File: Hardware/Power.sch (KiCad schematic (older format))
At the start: 24 parts, among them U601 PAM2306AYPAA, U603 LDO-X2SON-1.2V, U604 LDO-X2SON-3.3V, U605 LDO-X2SON-2.5V

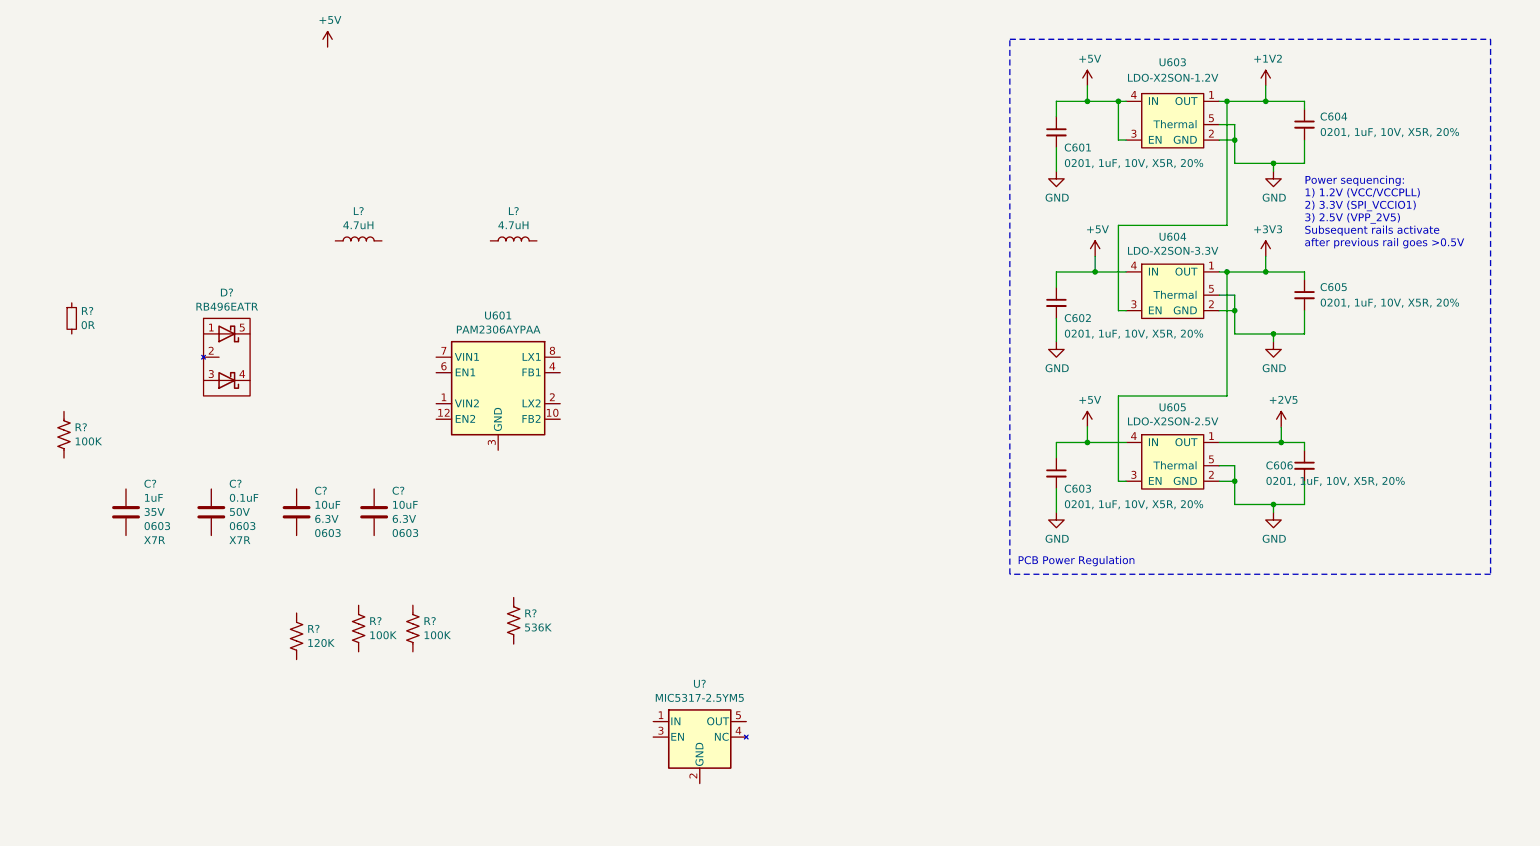
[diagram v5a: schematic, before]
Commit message: Prospecting the layout of AFE, detailing connectors to larger board size.
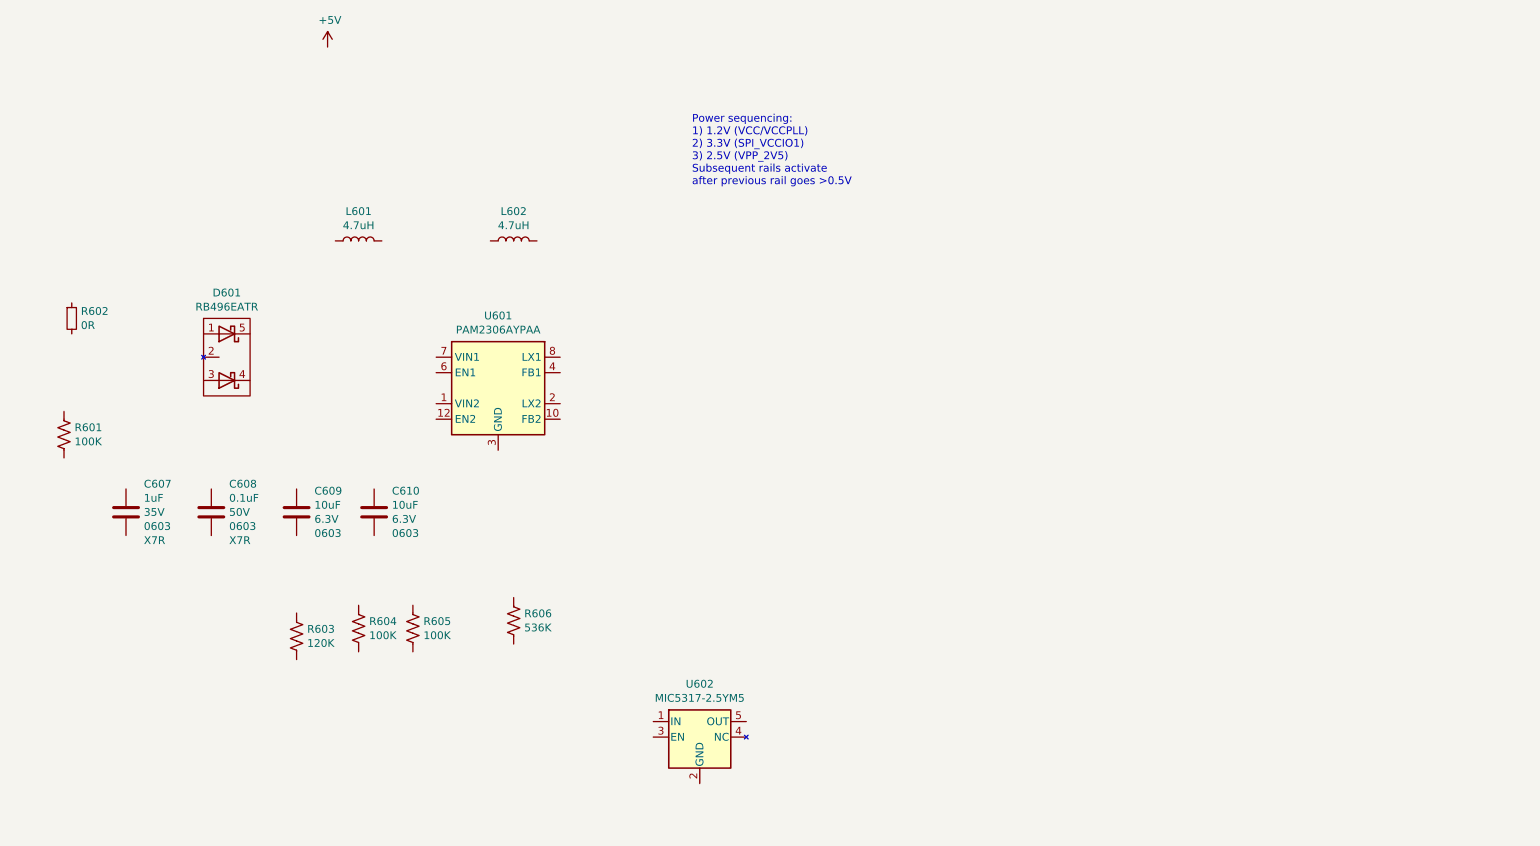
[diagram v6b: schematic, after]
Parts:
- removed C601, C602, C603, C604, C605, C606: 0201, 1uF, 10V, X5R, 20%, tomu-fpga:C_0201_0603Metric, symbol Device:C_Small
- removed U603: LDO-X2SON-1.2V, tomu-fpga:Texas_X2SON-4_1x1mm_P0.65mm, symbol tomu-fpga:LDO-X2SON
- removed U604: LDO-X2SON-3.3V, tomu-fpga:Texas_X2SON-4_1x1mm_P0.65mm, symbol tomu-fpga:LDO-X2SON
- removed U605: LDO-X2SON-2.5V, tomu-fpga:Texas_X2SON-4_1x1mm_P0.65mm, symbol tomu-fpga:LDO-X2SON
- gave numbers to parts that had none: 14
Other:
- note removed: "PCB Power Regulation"

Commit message: Power connectivity going in.
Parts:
- added C?: 10uF, Capacitor_SMD:C_0603_1608Metric, symbol Device:C
- R601: symbol Device:R_US -> Device:R_Small_US
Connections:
- net +5V: now also D601.4 (K2), D601.5 (K1), R601.1, U601.1 (VIN2), U601.6 (EN1), U601.7 (VIN1), C?.2
- net FB2: now reaches U601.10 (FB2)
- net FB2: now also R603.1, R606.2
- net at U601.12 (EN2): now also C607.1, R601.2
- net GND: now reaches U601.13 (GND), U601.3 (GND), U601.9 (GND)
- net GND: now also C607.2, C609.2, C610.2, R603.2, R605.2, U602.2 (GND), C?.1
- net at U601.2 (LX2): now also L602.1
- net FB1: now reaches U601.4 (FB1)
- net FB1: now also R604.2, R605.1
- net at U601.8 (LX1): now also L601.1
- net +1V2: now reaches L601.2
- net +1V2: now also C609.1, R604.1
- net +3V3: now reaches L602.2
- net +3V3: now also C610.1, R606.1
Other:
- moved on the sheet: C607, C608, C609, C610, D601, L601, L602, R603, R604, R605, R606

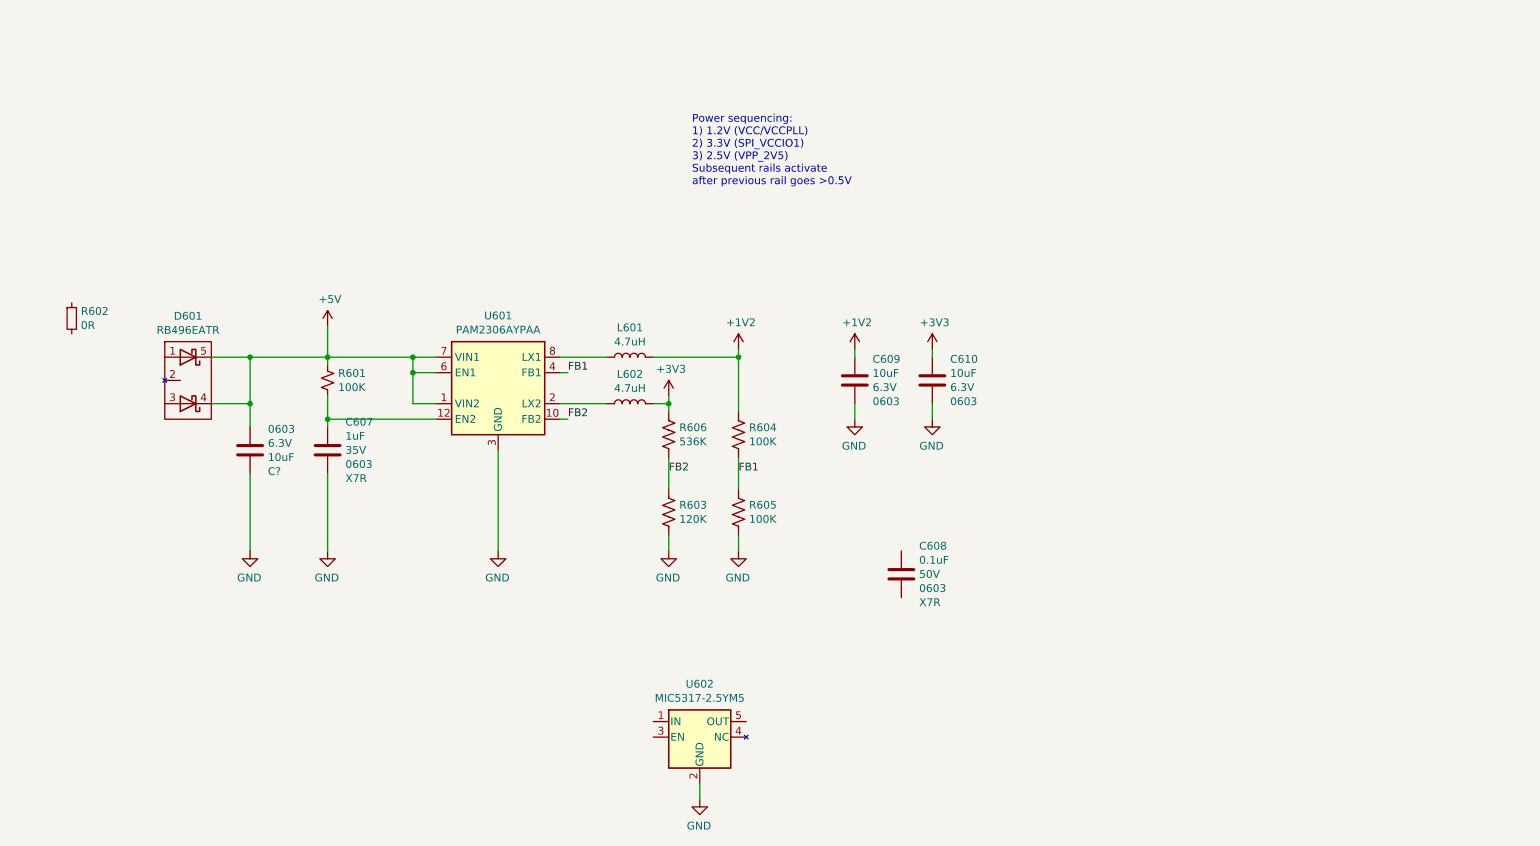
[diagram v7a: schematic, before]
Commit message: Putting in some connectivity. More passives.
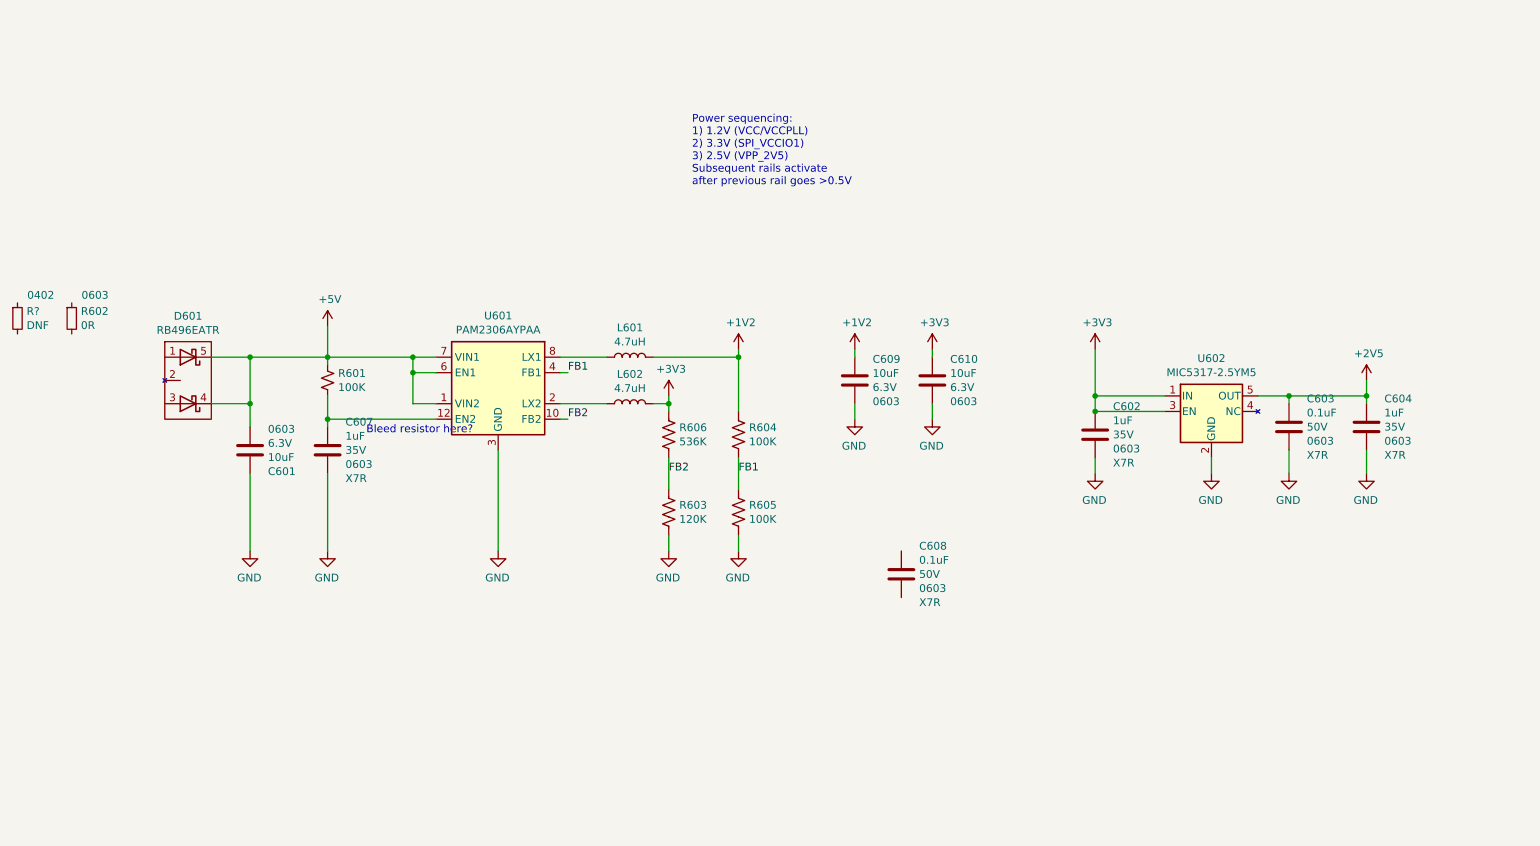
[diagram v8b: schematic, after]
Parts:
- added C602, C604: 1uF, Capacitor_SMD:C_0603_1608Metric, symbol Device:C
- added C603: 0.1uF, Capacitor_SMD:C_0603_1608Metric, symbol Device:C
- added R?: DNF, Resistor_SMD:R_0402_1005Metric, symbol Device:R_Small
- gave numbers to parts that had none: 1
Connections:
- net +3V3: now also U602.1 (IN), U602.3 (EN), C602.1
- net GND: now also C602.2, C603.2, C604.2
- net +2V5: now reaches U602.5 (OUT)
- net +2V5: now also C603.1, C604.1
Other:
- note added: "Bleed resistor here?"
- moved on the sheet: U602
